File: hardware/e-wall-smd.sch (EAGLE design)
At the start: 66 parts, among them IC1 74HCT595D, IC2 74HCT595D, IC3 74HCT595D, IC4 74HCT595D, Q1 SI2302CDS, Q10 SI2302CDS, Q11 SI2302CDS, Q12 SI2302CDS, Q13 SI2302CDS, Q14 SI2302CDS, Q15 SI2302CDS, Q16 SI2302CDS, Q17 SI2302CDS, Q18 SI2302CDS, Q19 SI2302CDS, Q2 SI2302CDS, Q20 SI2302CDS, Q21 SI2302CDS, Q22 SI2302CDS, Q23 SI2302CDS, Q24 SI2302CDS, Q25 SI4214DDY, Q26 SI4214DDY, Q27 SI4214DDY, Q28 SI4214DDY, Q29 SI2302CDS, Q3 SI2302CDS, Q30 SI2302CDS, Q31 SI2347DS, Q4 SI2302CDS, Q5 SI2302CDS, Q6 SI2302CDS, Q7 SI2302CDS, Q8 SI2302CDS, Q9 SI2302CDS

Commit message: kleine Anpassungen im Schema, erc bereinigt
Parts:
- SV1, SV2, SV3: value (none) -> 8x2
- SV4, SV5: value (none) -> 4x2
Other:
- moved on the sheet: D1, D10, D11, D12, D2, D3, D4, D5, D6, D7, D8, D9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

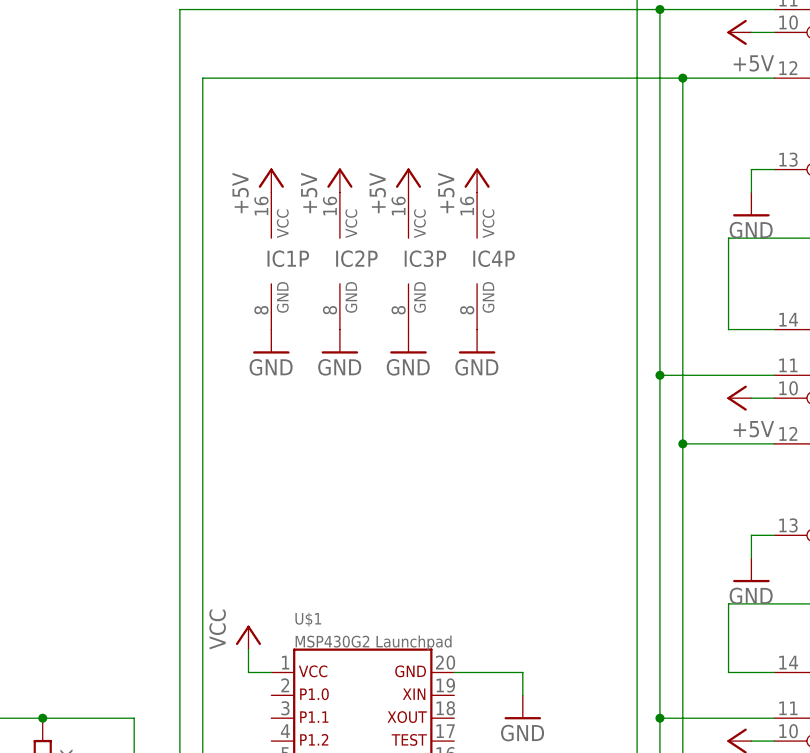
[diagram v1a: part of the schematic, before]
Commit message: Kondensatoren ergänzt
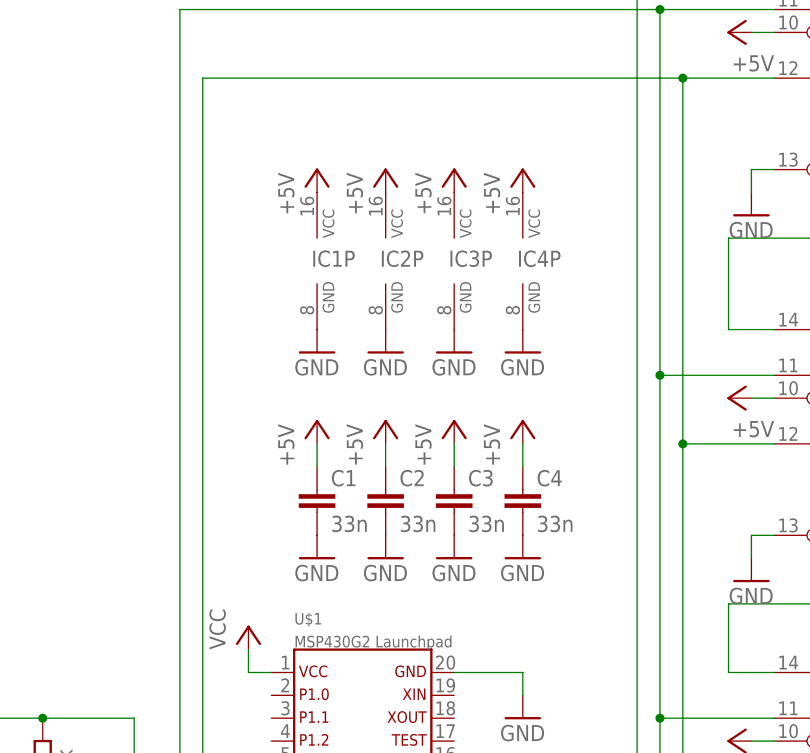
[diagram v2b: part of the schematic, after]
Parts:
- added C1, C2, C3, C4: 33n, resistor:C-EUC1206
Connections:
- net +5V: now also C1.1, C2.1, C3.1, C4.1
- net GND: now also C1.2, C2.2, C3.2, C4.2
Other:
- moved on the sheet: IC1P, IC2P, IC3P, IC4P
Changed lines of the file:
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@@
 <setting verticaltext="up"/>
 </settings>
-<grid distance="0.5" unitdist="inch" unit="inch" style="lines" multiple="1" display="no" altdistance="0.01" altunitdist="inch" altunit="inch"/>
+<grid distance="0.1" unitdist="inch" unit="inch" style="lines" multiple="1" display="no" altdistance="0.01" altunitdist="inch" altunit="inch"/>
 <layers>
 <layer number="1" name="Top" color="4" fill="1" visible="no" active="no"/>
@@
 <part name="GND49" library="supply1" deviceset="GND" device=""/>
 <part name="GND50" library="supply1" deviceset="GND" device=""/>
+<part name="C1" library="resistor" deviceset="C-EU" device="C1206" value="33n"/>
+<part name="C2" library="resistor" deviceset="C-EU" device="C1206" value="33n"/>
+<part name="C3" library="resistor" deviceset="C-EU" device="C1206" value="33n"/>
+<part name="C4" library="resistor" deviceset="C-EU" device="C1206" value="33n"/>
+<part name="GND51" library="supply1" deviceset="GND" device=""/>
+<part name="GND52" library="supply1" deviceset="GND" device=""/>
+<part name="GND53" library="supply1" deviceset="GND" device=""/>
+<part name="GND54" library="supply1" deviceset="GND" device=""/>
+<part name="P+28" library="supply1" deviceset="+5V" device=""/>
+<part name="P+29" library="supply1" deviceset="+5V" device=""/>
+<part name="P+30" library="supply1" deviceset="+5V" device=""/>
+<part name="P+31" library="supply1" deviceset="+5V" device=""/>
 </parts>
 <sheets>
@@
 <instance part="SV4" gate="G$1" x="408.94" y="33.02"/>
 <instance part="SV5" gate="G$1" x="408.94" y="12.7"/>
-<instance part="P+20" gate="1" x="68.58" y="129.54"/>
+<instance part="P+20" gate="1" x="73.66" y="129.54"/>
 <instance part="P+6" gate="1" x="33.02" y="99.06"/>
 <instance part="P+21" gate="1" x="17.78" y="99.06"/>
@@
 <instance part="P+3" gate="1" x="119.38" y="66.04" rot="R90"/>
 <instance part="P+19" gate="1" x="119.38" y="27.94" rot="R90"/>
-<instance part="IC1" gate="P" x="68.58" y="119.38"/>
-<instance part="IC2" gate="P" x="76.2" y="119.38"/>
-<instance part="IC3" gate="P" x="83.82" y="119.38"/>
-<instance part="IC4" gate="P" x="91.44" y="119.38"/>
-<instance part="GND44" gate="1" x="68.58" y="109.22"/>
-<instance part="GND45" gate="1" x="76.2" y="109.22"/>
-<instance part="GND46" gate="1" x="83.82" y="109.22"/>
-<instance part="GND47" gate="1" x="91.44" y="109.22"/>
-<instance part="P+23" gate="1" x="76.2" y="129.54"/>
-<instance part="P+24" gate="1" x="83.82" y="129.54"/>
-<instance part="P+25" gate="1" x="91.44" y="129.54"/>
+<instance part="IC1" gate="P" x="73.66" y="119.38"/>
+<instance part="IC2" gate="P" x="81.28" y="119.38"/>
+<instance part="IC3" gate="P" x="88.9" y="119.38"/>
+<instance part="IC4" gate="P" x="96.52" y="119.38"/>
+<instance part="GND44" gate="1" x="73.66" y="109.22"/>
+<instance part="GND45" gate="1" x="81.28" y="109.22"/>
+<instance part="GND46" gate="1" x="88.9" y="109.22"/>
+<instance part="GND47" gate="1" x="96.52" y="109.22"/>
+<instance part="P+23" gate="1" x="81.28" y="129.54"/>
+<instance part="P+24" gate="1" x="88.9" y="129.54"/>
+<instance part="P+25" gate="1" x="96.52" y="129.54"/>
 <instance part="TP1" gate="G$1" x="-10.16" y="30.48" rot="R270"/>
 <instance part="TP2" gate="G$1" x="15.24" y="127"/>
@@
 <instance part="GND49" gate="1" x="43.18" y="55.88"/>
 <instance part="GND50" gate="1" x="33.02" y="7.62"/>
+<instance part="C1" gate="G$1" x="73.66" y="93.98"/>
+<instance part="C2" gate="G$1" x="81.28" y="93.98"/>
+<instance part="C3" gate="G$1" x="88.9" y="93.98"/>
+<instance part="C4" gate="G$1" x="96.52" y="93.98"/>
+<instance part="GND51" gate="1" x="73.66" y="86.36"/>
+<instance part="GND52" gate="1" x="81.28" y="86.36"/>
+<instance part="GND53" gate="1" x="88.9" y="86.36"/>
+<instance part="GND54" gate="1" x="96.52" y="86.36"/>
+<instance part="P+28" gate="1" x="73.66" y="101.6"/>
+<instance part="P+29" gate="1" x="81.28" y="101.6"/>
+<instance part="P+30" gate="1" x="88.9" y="101.6"/>
+<instance part="P+31" gate="1" x="96.52" y="101.6"/>
 </instances>
 <busses>
@@
 <pinref part="P+26" gate="1" pin="+5V"/>
 </segment>
+<segment>
+<pinref part="C1" gate="G$1" pin="1"/>
+<pinref part="P+28" gate="1" pin="+5V"/>
+<wire x1="73.66" y1="99.06" x2="73.66" y2="96.52" width="0.1524" layer="91"/>
+</segment>
+<segment>
+<pinref part="C2" gate="G$1" pin="1"/>
+<pinref part="P+29" gate="1" pin="+5V"/>
+<wire x1="81.28" y1="99.06" x2="81.28" y2="96.52" width="0.1524" layer="91"/>
+</segment>
+<segment>
+<pinref part="C3" gate="G$1" pin="1"/>
+<pinref part="P+30" gate="1" pin="+5V"/>
+<wire x1="88.9" y1="99.06" x2="88.9" y2="96.52" width="0.1524" layer="91"/>
+</segment>
+<segment>
+<pinref part="C4" gate="G$1" pin="1"/>
+<pinref part="P+31" gate="1" pin="+5V"/>
+<wire x1="96.52" y1="99.06" x2="96.52" y2="96.52" width="0.1524" layer="91"/>
+</segment>
 </net>
 <net name="GND" class="0">
@@
 <wire x1="22.86" y1="10.16" x2="22.86" y2="17.78" width="0.1524" layer="91"/>
 </segment>
-</net>
+<segment>
+<pinref part="C1" gate="G$1" pin="2"/>
+<pinref part="GND51" gate="1" pin="GND"/>
+</segment>
+<segment>
+<pinref part="C2" gate="G$1" pin="2"/>
+<pinref part="GND52" gate="1" pin="GND"/>
+</segment>
+<segment>
+<pinref part="C3" gate="G$1" pin="2"/>
+<pinref part="GND53" gate="1" pin="GND"/>
+</segment>
+<segment>
+<pinref part="C4" gate="G$1" pin="2"/>
+<pinref part="GND54" gate="1" pin="GND"/>
+</segment>
+</net>

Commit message: Freilaufdioden bei Hochstromausgängen
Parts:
- added D13, D14, D15, D16: BAS40-05, diode:BAS40-05
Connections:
- net +12V: now also D13.C, D14.C, D15.C, D16.C
- net OUT24: now also D13.A1
- net OUT25: now also D13.A2
- net OUT26: now also D14.A1
- net OUT27: now also D14.A2
- net OUT28: now also D15.A1
- net OUT29: now also D15.A2
- net OUT30: now also D16.A1
- net OUT31: now also D16.A2
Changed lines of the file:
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@@
 <setting verticaltext="up"/>
 </settings>
-<grid distance="0.1" unitdist="inch" unit="inch" style="lines" multiple="1" display="no" altdistance="0.01" altunitdist="inch" altunit="inch"/>
+<grid distance="0.1" unitdist="inch" unit="inch" style="dots" multiple="1" display="yes" altdistance="0.01" altunitdist="inch" altunit="inch"/>
 <layers>
 <layer number="1" name="Top" color="4" fill="1" visible="no" active="no"/>
@@
 <part name="P+30" library="supply1" deviceset="+5V" device=""/>
 <part name="P+31" library="supply1" deviceset="+5V" device=""/>
+<part name="D13" library="diode" deviceset="BAS40-05" device=""/>
+<part name="D14" library="diode" deviceset="BAS40-05" device=""/>
+<part name="D15" library="diode" deviceset="BAS40-05" device=""/>
+<part name="D16" library="diode" deviceset="BAS40-05" device=""/>
+<part name="P+32" library="supply1" deviceset="+12V" device=""/>
+<part name="P+33" library="supply1" deviceset="+12V" device=""/>
+<part name="P+34" library="supply1" deviceset="+12V" device=""/>
+<part name="P+35" library="supply1" deviceset="+12V" device=""/>
 </parts>
 <sheets>
@@
 <instance part="P+30" gate="1" x="88.9" y="101.6"/>
 <instance part="P+31" gate="1" x="96.52" y="101.6"/>
+<instance part="D13" gate="G$1" x="360.68" y="139.7" rot="R270"/>
+<instance part="D14" gate="G$1" x="360.68" y="104.14" rot="R270"/>
+<instance part="D15" gate="G$1" x="360.68" y="68.58" rot="R270"/>
+<instance part="D16" gate="G$1" x="360.68" y="33.02" rot="R270"/>
+<instance part="P+32" gate="1" x="363.22" y="142.24"/>
+<instance part="P+33" gate="1" x="363.22" y="106.68"/>
+<instance part="P+34" gate="1" x="363.22" y="71.12"/>
+<instance part="P+35" gate="1" x="363.22" y="35.56"/>
 </instances>
 <busses>
@@
 <pinref part="P+27" gate="1" pin="+12V"/>
 </segment>
+<segment>
+<pinref part="D13" gate="G$1" pin="C"/>
+<pinref part="P+32" gate="1" pin="+12V"/>
+</segment>
+<segment>
+<pinref part="D14" gate="G$1" pin="C"/>
+<pinref part="P+33" gate="1" pin="+12V"/>
+</segment>
+<segment>
+<pinref part="D15" gate="G$1" pin="C"/>
+<pinref part="P+34" gate="1" pin="+12V"/>
+</segment>
+<segment>
+<pinref part="D16" gate="G$1" pin="C"/>
+<pinref part="P+35" gate="1" pin="+12V"/>
+</segment>
 </net>
 <net name="SOMI_UC" class="0">
@@
 <wire x1="365.76" y1="147.32" x2="368.3" y2="149.86" width="0.1524" layer="91"/>
 <pinref part="Q25" gate="B" pin="D"/>
-<wire x1="365.76" y1="147.32" x2="340.36" y2="147.32" width="0.1524" layer="91"/>
+<wire x1="365.76" y1="147.32" x2="360.68" y2="147.32" width="0.1524" layer="91"/>
 <label x="342.9" y="147.32" size="1.778" layer="95"/>
+<pinref part="D13" gate="G$1" pin="A1"/>
+<wire x1="360.68" y1="147.32" x2="340.36" y2="147.32" width="0.1524" layer="91"/>
+<wire x1="360.68" y1="144.78" x2="360.68" y2="147.32" width="0.1524" layer="91"/>
+<junction x="360.68" y="147.32"/>
 </segment>
 <segment>
@@
 <wire x1="365.76" y1="129.54" x2="368.3" y2="132.08" width="0.1524" layer="91"/>
 <pinref part="Q25" gate="A" pin="D"/>
-<wire x1="365.76" y1="129.54" x2="340.36" y2="129.54" width="0.1524" layer="91"/>
+<wire x1="365.76" y1="129.54" x2="360.68" y2="129.54" width="0.1524" layer="91"/>
 <label x="342.9" y="129.54" size="1.778" layer="95"/>
+<pinref part="D13" gate="G$1" pin="A2"/>
+<wire x1="360.68" y1="129.54" x2="340.36" y2="129.54" width="0.1524" layer="91"/>
+<wire x1="360.68" y1="134.62" x2="360.68" y2="129.54" width="0.1524" layer="91"/>
+<junction x="360.68" y="129.54"/>
 </segment>
 <segment>
@@
 <wire x1="365.76" y1="111.76" x2="368.3" y2="114.3" width="0.1524" layer="91"/>
 <pinref part="Q26" gate="B" pin="D"/>
-<wire x1="340.36" y1="111.76" x2="365.76" y2="111.76" width="0.1524" layer="91"/>
+<wire x1="340.36" y1="111.76" x2="360.68" y2="111.76" width="0.1524" layer="91"/>
 <label x="342.9" y="111.76" size="1.778" layer="95"/>
+<pinref part="D14" gate="G$1" pin="A1"/>
+<wire x1="360.68" y1="111.76" x2="365.76" y2="111.76" width="0.1524" layer="91"/>
+<wire x1="360.68" y1="109.22" x2="360.68" y2="111.76" width="0.1524" layer="91"/>
+<junction x="360.68" y="111.76"/>
 </segment>
 <segment>
@@
 <wire x1="365.76" y1="93.98" x2="368.3" y2="96.52" width="0.1524" layer="91"/>
 <pinref part="Q26" gate="A" pin="D"/>
-<wire x1="340.36" y1="93.98" x2="365.76" y2="93.98" width="0.1524" layer="91"/>
+<wire x1="340.36" y1="93.98" x2="360.68" y2="93.98" width="0.1524" layer="91"/>
 <label x="342.9" y="93.98" size="1.778" layer="95"/>
+<pinref part="D14" gate="G$1" pin="A2"/>
+<wire x1="360.68" y1="93.98" x2="365.76" y2="93.98" width="0.1524" layer="91"/>
+<wire x1="360.68" y1="99.06" x2="360.68" y2="93.98" width="0.1524" layer="91"/>
+<junction x="360.68" y="93.98"/>
 </segment>
 <segment>
@@
 <wire x1="365.76" y1="76.2" x2="368.3" y2="78.74" width="0.1524" layer="91"/>
 <pinref part="Q27" gate="B" pin="D"/>
-<wire x1="340.36" y1="76.2" x2="365.76" y2="76.2" width="0.1524" layer="91"/>
+<wire x1="340.36" y1="76.2" x2="360.68" y2="76.2" width="0.1524" layer="91"/>
 <label x="342.9" y="76.2" size="1.778" layer="95"/>
+<pinref part="D15" gate="G$1" pin="A1"/>
+<wire x1="360.68" y1="76.2" x2="365.76" y2="76.2" width="0.1524" layer="91"/>
+<wire x1="360.68" y1="73.66" x2="360.68" y2="76.2" width="0.1524" layer="91"/>
+<junction x="360.68" y="76.2"/>
 </segment>
 <segment>
@@
 <wire x1="365.76" y1="58.42" x2="368.3" y2="60.96" width="0.1524" layer="91"/>
 <pinref part="Q27" gate="A" pin="D"/>
-<wire x1="340.36" y1="58.42" x2="365.76" y2="58.42" width="0.1524" layer="91"/>
+<wire x1="340.36" y1="58.42" x2="360.68" y2="58.42" width="0.1524" layer="91"/>
 <label x="342.9" y="58.42" size="1.778" layer="95"/>
+<pinref part="D15" gate="G$1" pin="A2"/>
+<wire x1="360.68" y1="58.42" x2="365.76" y2="58.42" width="0.1524" layer="91"/>
+<wire x1="360.68" y1="63.5" x2="360.68" y2="58.42" width="0.1524" layer="91"/>
+<junction x="360.68" y="58.42"/>
 </segment>
 <segment>
@@
 <wire x1="365.76" y1="40.64" x2="368.3" y2="43.18" width="0.1524" layer="91"/>
 <pinref part="Q28" gate="B" pin="D"/>
-<wire x1="365.76" y1="40.64" x2="340.36" y2="40.64" width="0.1524" layer="91"/>
+<wire x1="365.76" y1="40.64" x2="360.68" y2="40.64" width="0.1524" layer="91"/>
 <label x="342.9" y="40.64" size="1.778" layer="95"/>
+<pinref part="D16" gate="G$1" pin="A1"/>
+<wire x1="360.68" y1="40.64" x2="340.36" y2="40.64" width="0.1524" layer="91"/>
+<wire x1="360.68" y1="38.1" x2="360.68" y2="40.64" width="0.1524" layer="91"/>
+<junction x="360.68" y="40.64"/>
 </segment>
 <segment>
@@
 <wire x1="365.76" y1="22.86" x2="368.3" y2="25.4" width="0.1524" layer="91"/>
 <pinref part="Q28" gate="A" pin="D"/>
-<wire x1="365.76" y1="22.86" x2="340.36" y2="22.86" width="0.1524" layer="91"/>
+<wire x1="365.76" y1="22.86" x2="360.68" y2="22.86" width="0.1524" layer="91"/>
 <label x="342.9" y="22.86" size="1.778" layer="95"/>
-</segment>
-<segment>
+<pinref part="D16" gate="G$1" pin="A2"/>
+<wire x1="360.68" y1="22.86" x2="340.36" y2="22.86" width="0.1524" layer="91"/>
+<wire x1="360.68" y1="27.94" x2="360.68" y2="22.86" width="0.1524" layer="91"/>
+<junction x="360.68" y="22.86"/>
+</segment>
+<segment>

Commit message: Separate polygons for signal and power ground
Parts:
- added R5: 0, resistor:R-EU_R1206
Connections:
- new net PWR_GND: Q1.S, Q10.S, Q11.S, Q12.S, Q13.S, Q14.S, Q15.S, Q16.S, Q17.S, Q18.S, Q19.S, Q2.S, Q20.S, Q21.S, Q22.S, Q23.S, Q24.S, Q25A.S, Q25B.S, Q26A.S, Q26B.S, Q27A.S, Q27B.S, Q28A.S, Q28B.S, Q3.S, Q4.S, Q5.S, Q6.S, Q7.S, Q8.S, Q9.S, R5.1, TP4.TP
- net GND: now also R5.2; no longer Q1.S, Q10.S, Q11.S, Q12.S, Q13.S, Q14.S, Q15.S, Q16.S, Q17.S, Q18.S, Q19.S, Q2.S, Q20.S, Q21.S, Q22.S, Q23.S, Q24.S, Q25A.S, Q25B.S, Q26A.S, Q26B.S, Q27A.S, Q27B.S, Q28A.S, Q28B.S, Q3.S, Q4.S, Q5.S, Q6.S, Q7.S, Q8.S, Q9.S, TP4.TP
